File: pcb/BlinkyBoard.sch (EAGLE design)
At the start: 21 parts, among them Q1 16 MHz

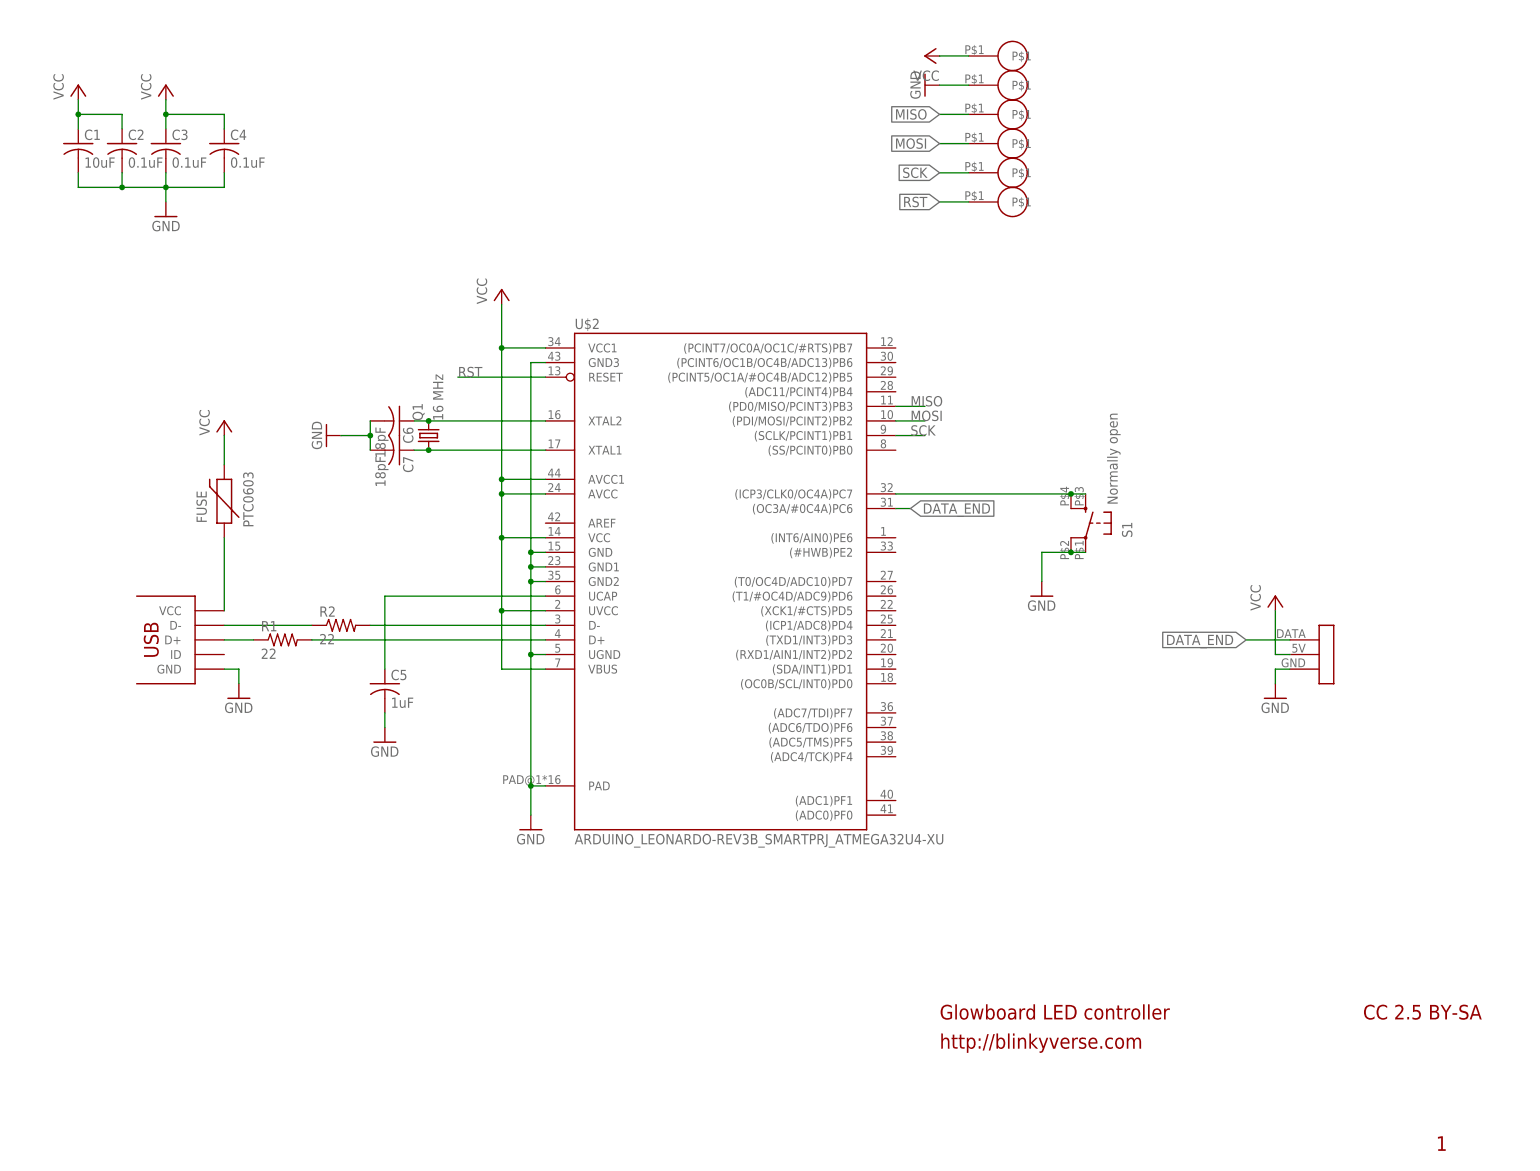
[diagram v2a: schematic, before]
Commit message: Add chopped version of 32u4 package, for BB RevB
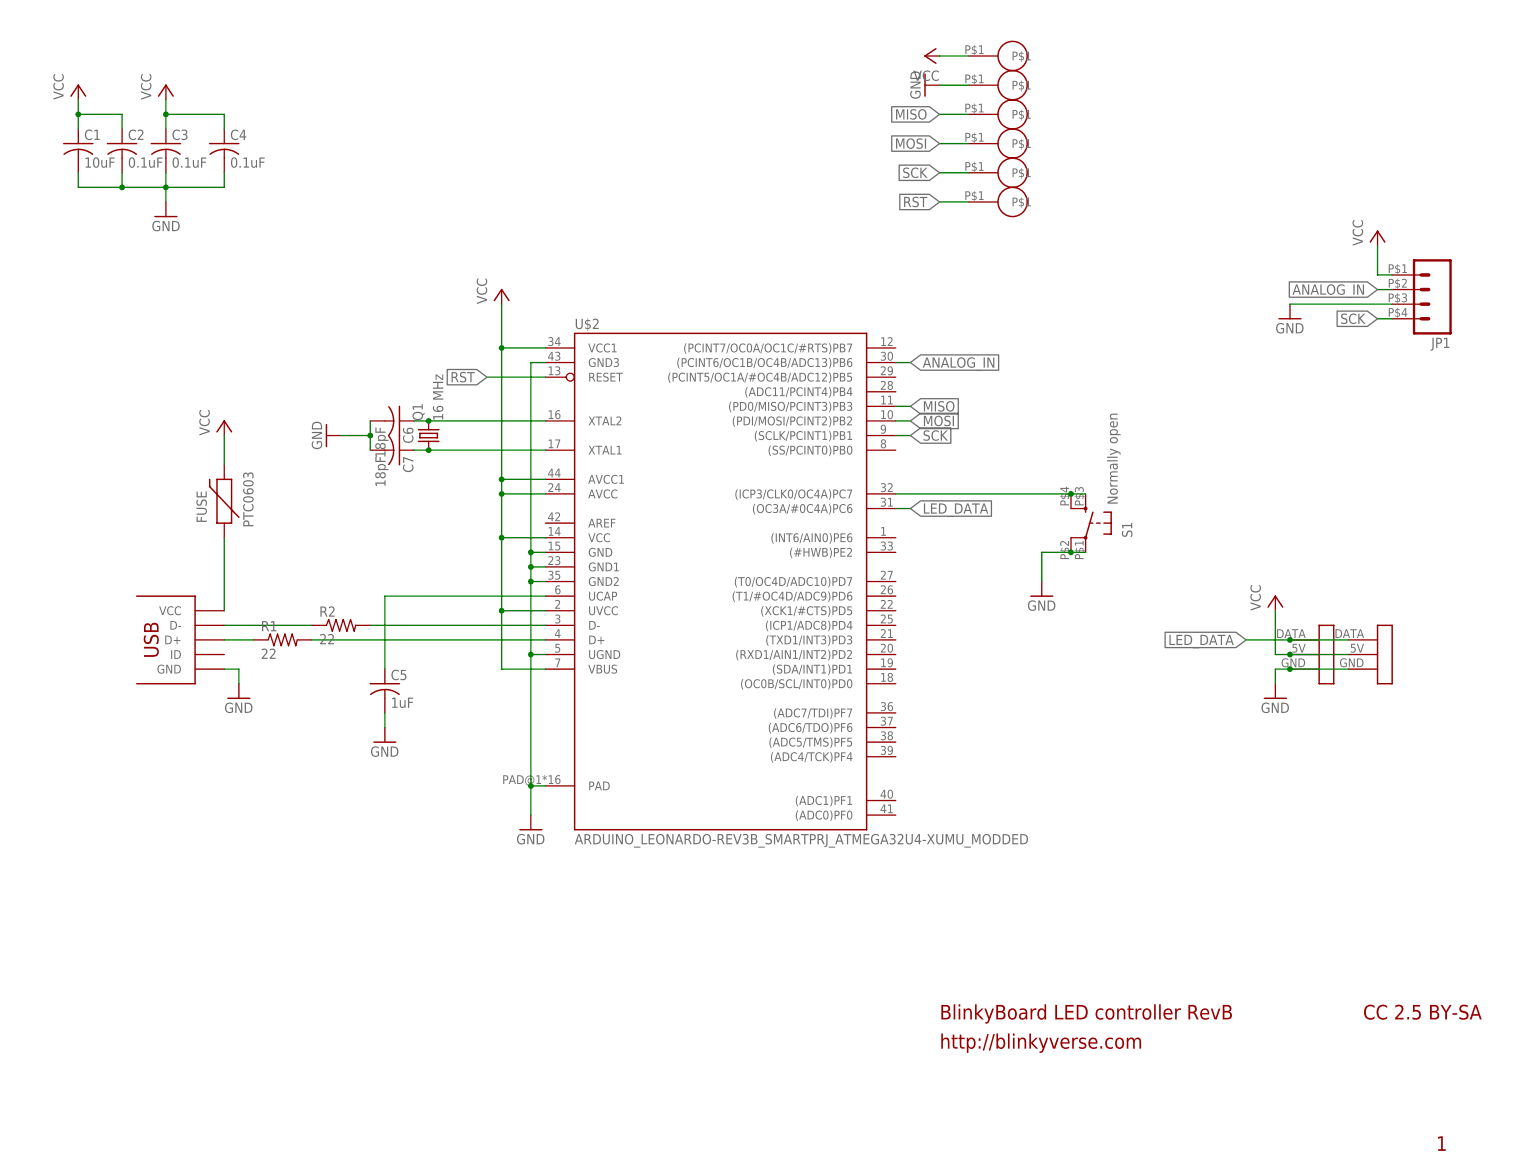
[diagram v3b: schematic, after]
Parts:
- added JP1: (no value), blinkiverse:M04
- added WS3: WS2811_CONNECTOR, blinkiverse:WS2811_CONNECTOR
- U$2: value ARDUINO_LEONARDO-REV3B_SMARTPRJ_ATMEGA32U4-XU -> ARDUINO_LEONARDO-REV3B_SMARTPRJ_ATMEGA32U4-XUMU_MODDED; device blinkiverse:ARDUINO_LEONARDO-REV3B_SMARTPRJ_ATMEGA32U4-XU -> blinkiverse:ARDUINO_LEONARDO-REV3B_SMARTPRJ_ATMEGA32U4-XUMU_MODDED
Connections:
- removed net DATA_END: U$2.(OC3A/#0C4A)PC6, WS1.DATA
- new net ANALOG_IN: JP1.2, U$2.(PCINT6/OC1B/OC4B/ADC13)PB6
- new net LED_DATA: U$2.(OC3A/#0C4A)PC6, WS1.DATA, WS3.DATA
- net GND: now also JP1.3, WS3.GND
- net SCK: now also JP1.4
- net VCC: now also JP1.1, WS3.5V
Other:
- note added: "BlinkyBoard LED controller RevB"
- note removed: "Glowboard LED controller"
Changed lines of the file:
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@@
 <setting verticaltext="up"/>
 </settings>
-<grid distance="0.1" unitdist="inch" unit="inch" style="lines" multiple="1" display="yes" altdistance="0.01" altunitdist="inch" altunit="inch"/>
+<grid distance="0.1" unitdist="inch" unit="inch" style="lines" multiple="1" display="no" altdistance="0.01" altunitdist="inch" altunit="inch"/>
 <layers>
 <layer number="1" name="Top" color="4" fill="1" visible="no" active="no"/>
@@
 <part name="P+1" library="supply1" deviceset="VCC" device=""/>
 <part name="FRAME1" library="frames" deviceset="FRAME_A_L" device=""/>
-<part name="U$2" library="blinkiverse" deviceset="ARDUINO_LEONARDO-REV3B_SMARTPRJ_ATMEGA32U4-XU" device="" value="ARDUINO_LEONARDO-REV3B_SMARTPRJ_ATMEGA32U4-XU"/>
+<part name="U$2" library="blinkiverse" deviceset="ARDUINO_LEONARDO-REV3B_SMARTPRJ_ATMEGA32U4-XU" device="MU_MODDED" value="ARDUINO_LEONARDO-REV3B_SMARTPRJ_ATMEGA32U4-XUMU_MODDED"/>
 <part name="GND8" library="supply1" deviceset="GND" device=""/>
 <part name="P+6" library="supply1" deviceset="VCC" device=""/>
@@
 <part name="P+2" library="supply1" deviceset="VCC" device=""/>
 <part name="GND1" library="supply1" deviceset="GND" device=""/>
+<part name="GND2" library="supply1" deviceset="GND" device=""/>
+<part name="WS3" library="blinkiverse" deviceset="WS2811_CONNECTOR" device=""/>
+<part name="JP1" library="blinkiverse" deviceset="M04" device=""/>
+<part name="P+5" library="supply1" deviceset="VCC" device=""/>
 </parts>
 <sheets>
 <sheet>
 <plain>
-<text x="104.14" y="-30.48" size="2.54" layer="94">Glowboard LED controller</text>
+<text x="104.14" y="-30.48" size="2.54" layer="94">BlinkyBoard LED controller RevB</text>
 <text x="104.14" y="-35.56" size="2.54" layer="94">http://blinkyverse.com</text>
 <text x="177.8" y="-30.48" size="2.54" layer="94">CC 2.5 BY-SA</text>
@@
 <instance part="P+2" gate="VCC" x="101.6" y="137.16" rot="R90"/>
 <instance part="GND1" gate="1" x="101.6" y="132.08" rot="R270"/>
+<instance part="GND2" gate="1" x="165.1" y="91.44"/>
+<instance part="WS3" gate="G$1" x="182.88" y="33.02"/>
+<instance part="JP1" gate="G$1" x="187.96" y="96.52" rot="R180"/>
+<instance part="P+5" gate="VCC" x="180.34" y="106.68"/>
 </instances>
 <busses>
@@
 <pinref part="GND4" gate="1" pin="GND"/>
 <wire x1="162.56" y1="30.48" x2="162.56" y2="27.94" width="0.1524" layer="91"/>
+<pinref part="WS3" gate="G$1" pin="GND"/>
+<wire x1="175.26" y1="30.48" x2="165.1" y2="30.48" width="0.1524" layer="91"/>
+<junction x="165.1" y="30.48"/>
 </segment>
 <segment>
@@
 <wire x1="104.14" y1="132.08" x2="109.22" y2="132.08" width="0.1524" layer="91"/>
 </segment>
+<segment>
+<pinref part="GND2" gate="1" pin="GND"/>
+<wire x1="165.1" y1="93.98" x2="182.88" y2="93.98" width="0.1524" layer="91"/>
+<pinref part="JP1" gate="G$1" pin="3"/>
+</segment>
 </net>
 <net name="MOSI" class="0">
 <segment>
 <pinref part="U$2" gate="G$1" pin="(PDI/MOSI/PCINT2)PB2"/>
-<wire x1="96.52" y1="73.66" x2="101.6" y2="73.66" width="0.1524" layer="91"/>
-<label x="99.06" y="73.66" size="1.778" layer="95"/>
+<wire x1="96.52" y1="73.66" x2="99.06" y2="73.66" width="0.1524" layer="91"/>
+<label x="99.06" y="73.66" size="1.778" layer="95" xref="yes"/>
 </segment>
 <segment>
@@
 <segment>
 <pinref part="U$2" gate="G$1" pin="(PD0/MISO/PCINT3)PB3"/>
-<wire x1="96.52" y1="76.2" x2="101.6" y2="76.2" width="0.1524" layer="91"/>
-<label x="99.06" y="76.2" size="1.778" layer="95"/>
+<wire x1="96.52" y1="76.2" x2="99.06" y2="76.2" width="0.1524" layer="91"/>
+<label x="99.06" y="76.2" size="1.778" layer="95" xref="yes"/>
 </segment>
 <segment>
@@
 <segment>
 <pinref part="U$2" gate="G$1" pin="(SCLK/PCINT1)PB1"/>
-<wire x1="96.52" y1="71.12" x2="101.6" y2="71.12" width="0.1524" layer="91"/>
-<label x="99.06" y="71.12" size="1.778" layer="95"/>
+<wire x1="96.52" y1="71.12" x2="99.06" y2="71.12" width="0.1524" layer="91"/>
+<label x="99.06" y="71.12" size="1.778" layer="95" xref="yes"/>
 </segment>
 <segment>
@@
 <pinref part="U$5" gate="G$1" pin="P$1"/>
 </segment>
+<segment>
+<pinref part="JP1" gate="G$1" pin="4"/>
+<wire x1="182.88" y1="91.44" x2="180.34" y2="91.44" width="0.1524" layer="91"/>
+<label x="180.34" y="91.44" size="1.778" layer="95" rot="R180" xref="yes"/>
+</segment>
 </net>
 <net name="RST" class="0">
 <segment>
 <pinref part="U$2" gate="G$1" pin="RESET"/>
-<wire x1="35.56" y1="81.28" x2="20.32" y2="81.28" width="0.1524" layer="91"/>
-<label x="20.32" y="81.28" size="1.778" layer="95"/>
+<wire x1="35.56" y1="81.28" x2="25.4" y2="81.28" width="0.1524" layer="91"/>
+<label x="25.4" y="81.28" size="1.778" layer="95" rot="R180" xref="yes"/>
 </segment>
 <segment>
@@
 </segment>
 </net>
+<net name="D-" class="0">
+<segment>
+<pinref part="R2" gate="G$1" pin="2"/>
+<pinref part="U$2" gate="G$1" pin="D-"/>
+<wire x1="5.08" y1="38.1" x2="35.56" y2="38.1" width="0.1524" layer="91"/>
+</segment>
+</net>
+<net name="D+" class="0">
+<segment>
+<pinref part="U$2" gate="G$1" pin="D+"/>
+<pinref part="R1" gate="G$1" pin="2"/>
+<wire x1="35.56" y1="35.56" x2="-5.08" y2="35.56" width="0.1524" layer="91"/>
+</segment>
+</net>
+<net name="N$10" class="0">
+<segment>
+<pinref part="U$2" gate="G$1" pin="(ICP3/CLK0/OC4A)PC7"/>
+<pinref part="S1" gate="1" pin="S1"/>
+<wire x1="96.52" y1="60.96" x2="127" y2="60.96" width="0.1524" layer="91"/>
+<pinref part="S1" gate="1" pin="S"/>
+<wire x1="129.54" y1="60.96" x2="127" y2="60.96" width="0.1524" layer="91"/>
+<junction x="127" y="60.96"/>
+</segment>
+</net>
+<net name="N$1" class="0">
+<segment>
+<pinref part="FUSE" gate="G$1" pin="1"/>
+<pinref part="U$4" gate="G$1" pin="VCC"/>
+<wire x1="-20.32" y1="40.64" x2="-20.32" y2="53.34" width="0.1524" layer="91"/>
+</segment>
+</net>
+<net name="N$2" class="0">
+<segment>
+<pinref part="U$2" gate="G$1" pin="UCAP"/>
+<wire x1="35.56" y1="43.18" x2="7.62" y2="43.18" width="0.1524" layer="91"/>
+<pinref part="C5" gate="G$1" pin="1"/>
+<wire x1="7.62" y1="30.48" x2="7.62" y2="43.18" width="0.1524" layer="91"/>
+</segment>
+</net>
+<net name="ANALOG_IN" class="0">
+<segment>
+<pinref part="U$2" gate="G$1" pin="(PCINT6/OC1B/OC4B/ADC13)PB6"/>
+<wire x1="96.52" y1="83.82" x2="99.06" y2="83.82" width="0.1524" layer="91"/>
+<label x="99.06" y="83.82" size="1.778" layer="95" xref="yes"/>
+</segment>
+<segment>
+<label x="180.34" y="96.52" size="1.778" layer="95" rot="R180" xref="yes"/>
+<pinref part="JP1" gate="G$1" pin="2"/>
+<wire x1="182.88" y1="96.52" x2="180.34" y2="96.52" width="0.1524" layer="91"/>
+</segment>
+</net>
+<net name="LED_DATA" class="0">
+<segment>
+<pinref part="U$2" gate="G$1" pin="(OC3A/#0C4A)PC6"/>
+<wire x1="96.52" y1="58.42" x2="99.06" y2="58.42" width="0.1524" layer="91"/>
+<label x="99.06" y="58.42" size="1.778" layer="95" xref="yes"/>
+</segment>
+<segment>
+<pinref part="WS1" gate="G$1" pin="DATA"/>
+<wire x1="165.1" y1="35.56" x2="157.48" y2="35.56" width="0.1524" layer="91"/>
+<label x="157.48" y="35.56" size="1.778" layer="95" rot="R180" xref="yes"/>
+<pinref part="WS3" gate="G$1" pin="DATA"/>
+<wire x1="175.26" y1="35.56" x2="165.1" y2="35.56" width="0.1524" layer="91"/>
+<junction x="165.1" y="35.56"/>
+</segment>
+</net>
 <net name="VCC" class="0">
+<segment>
+<pinref part="JP1" gate="G$1" pin="1"/>
+<wire x1="182.88" y1="99.06" x2="180.34" y2="99.06" width="0.1524" layer="91"/>
+<wire x1="180.34" y1="99.06" x2="180.34" y2="104.14" width="0.1524" layer="91"/>
+<pinref part="P+5" gate="VCC" pin="VCC"/>
+</segment>
 <segment>
 <pinref part="C1" gate="G$1" pin="1"/>
@@
 <pinref part="P+3" gate="VCC" pin="VCC"/>
 <wire x1="162.56" y1="33.02" x2="162.56" y2="40.64" width="0.1524" layer="91"/>
+<pinref part="WS3" gate="G$1" pin="5V"/>
+<wire x1="165.1" y1="33.02" x2="175.26" y2="33.02" width="0.1524" layer="91"/>
+<junction x="165.1" y="33.02"/>
 </segment>
 <segment>
@@
 </segment>
 </net>
-<net name="D-" class="0">
-<segment>
-<pinref part="R2" gate="G$1" pin="2"/>
-<pinref part="U$2" gate="G$1" pin="D-"/>
-<wire x1="5.08" y1="38.1" x2="35.56" y2="38.1" width="0.1524" layer="91"/>
-</segment>
-</net>
-<net name="D+" class="0">
-<segment>
-<pinref part="U$2" gate="G$1" pin="D+"/>
-<pinref part="R1" gate="G$1" pin="2"/>
-<wire x1="35.56" y1="35.56" x2="-5.08" y2="35.56" width="0.1524" layer="91"/>
-</segment>
-</net>
-<net name="N$10" class="0">
-<segment>
-<pinref part="U$2" gate="G$1" pin="(ICP3/CLK0/OC4A)PC7"/>
-<pinref part="S1" gate="1" pin="S1"/>
-<wire x1="96.52" y1="60.96" x2="127" y2="60.96" width="0.1524" layer="91"/>
-<pinref part="S1" gate="1" pin="S"/>
-<wire x1="129.54" y1="60.96" x2="127" y2="60.96" width="0.1524" layer="91"/>
-<junction x="127" y="60.96"/>
-</segment>
-</net>
-<net name="N$1" class="0">
-<segment>
-<pinref part="FUSE" gate="G$1" pin="1"/>
-<pinref part="U$4" gate="G$1" pin="VCC"/>
-<wire x1="-20.32" y1="40.64" x2="-20.32" y2="53.34" width="0.1524" layer="91"/>
-</segment>
-</net>
-<net name="N$2" class="0">
-<segment>
-<pinref part="U$2" gate="G$1" pin="UCAP"/>
-<wire x1="35.56" y1="43.18" x2="7.62" y2="43.18" width="0.1524" layer="91"/>
-<pinref part="C5" gate="G$1" pin="1"/>
-<wire x1="7.62" y1="30.48" x2="7.62" y2="43.18" width="0.1524" layer="91"/>
-</segment>
-</net>
-<net name="DATA_END" class="0">
-<segment>
-<pinref part="WS1" gate="G$1" pin="DATA"/>
-<wire x1="165.1" y1="35.56" x2="157.48" y2="35.56" width="0.1524" layer="91"/>
-<label x="157.48" y="35.56" size="1.778" layer="95" rot="R180" xref="yes"/>
-</segment>
-<segment>
-<pinref part="U$2" gate="G$1" pin="(OC3A/#0C4A)PC6"/>
-<wire x1="96.52" y1="58.42" x2="99.06" y2="58.42" width="0.1524" layer="91"/>
-<label x="99.06" y="58.42" size="1.778" layer="95" xref="yes"/>
-</segment>
-</net>

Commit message: Fuses are for suckers.
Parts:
- removed FUSE: PTC0603, SparkFun-PowerIC:PTC0603
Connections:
- removed net N$1: FUSE.1, U$4.VCC
- net VCC: now also U$4.VCC; no longer FUSE.2
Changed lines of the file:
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@@
 <part name="P+3" library="supply1" deviceset="VCC" device=""/>
 <part name="GND4" library="supply1" deviceset="GND" device=""/>
-<part name="FUSE" library="SparkFun-PowerIC" deviceset="PTC" device="0603"/>
 <part name="P+4" library="supply1" deviceset="VCC" device=""/>
 <part name="U$4" library="blinkiverse" deviceset="MICRO_USB" device=""/>
@@
 <instance part="P+3" gate="VCC" x="162.56" y="43.18"/>
 <instance part="GND4" gate="1" x="162.56" y="25.4"/>
-<instance part="FUSE" gate="G$1" x="-20.32" y="58.42" rot="R90"/>
 <instance part="P+4" gate="VCC" x="-20.32" y="73.66"/>
 <instance part="U$4" gate="G$1" x="-27.94" y="35.56"/>
@@
 <instance part="P+2" gate="VCC" x="101.6" y="137.16" rot="R90"/>
 <instance part="GND1" gate="1" x="101.6" y="132.08" rot="R270"/>
-<instance part="GND2" gate="1" x="165.1" y="91.44"/>
+<instance part="GND2" gate="1" x="170.18" y="86.36"/>
 <instance part="WS3" gate="G$1" x="182.88" y="33.02"/>
 <instance part="JP1" gate="G$1" x="187.96" y="96.52" rot="R180"/>
@@
 </segment>
 <segment>
+<pinref part="JP1" gate="G$1" pin="3"/>
 <pinref part="GND2" gate="1" pin="GND"/>
-<wire x1="165.1" y1="93.98" x2="182.88" y2="93.98" width="0.1524" layer="91"/>
-<pinref part="JP1" gate="G$1" pin="3"/>
+<wire x1="182.88" y1="93.98" x2="170.18" y2="93.98" width="0.1524" layer="91"/>
+<wire x1="170.18" y1="93.98" x2="170.18" y2="88.9" width="0.1524" layer="91"/>
 </segment>
 </net>
@@
 </segment>
 <segment>
+<label x="180.34" y="91.44" size="1.778" layer="95" rot="R180" xref="yes"/>
 <pinref part="JP1" gate="G$1" pin="4"/>
-<wire x1="182.88" y1="91.44" x2="180.34" y2="91.44" width="0.1524" layer="91"/>
-<label x="180.34" y="91.44" size="1.778" layer="95" rot="R180" xref="yes"/>
+<wire x1="180.34" y1="91.44" x2="182.88" y2="91.44" width="0.1524" layer="91"/>
 </segment>
 </net>
@@
 <wire x1="129.54" y1="60.96" x2="127" y2="60.96" width="0.1524" layer="91"/>
 <junction x="127" y="60.96"/>
-</segment>
-</net>
-<net name="N$1" class="0">
-<segment>
-<pinref part="FUSE" gate="G$1" pin="1"/>
-<pinref part="U$4" gate="G$1" pin="VCC"/>
-<wire x1="-20.32" y1="40.64" x2="-20.32" y2="53.34" width="0.1524" layer="91"/>
 </segment>
 </net>
@@
 </segment>
 <segment>
-<pinref part="FUSE" gate="G$1" pin="2"/>
-<wire x1="-20.32" y1="66.04" x2="-20.32" y2="71.12" width="0.1524" layer="91"/>
 <pinref part="P+4" gate="VCC" pin="VCC"/>
-</segment>
-<segment>
+<pinref part="U$4" gate="G$1" pin="VCC"/>
+<wire x1="-20.32" y1="71.12" x2="-20.32" y2="40.64" width="0.1524" layer="91"/>
+</segment>
+<segment>

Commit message: PCB: replace smt USB connector with thru-hole version
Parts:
- removed JP1: (no value), blinkiverse:M04
- U$4: value MICRO_USB -> MICRO_USBSMT+DIP; device blinkiverse:MICRO_USB -> blinkiverse:MICRO_USBSMT+DIP
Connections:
- net ANALOG_IN: no longer JP1.2
- net GND: no longer JP1.3
- net SCK: no longer JP1.4
- net VCC: no longer JP1.1
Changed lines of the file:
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@@
 <part name="GND4" library="supply1" deviceset="GND" device=""/>
 <part name="P+4" library="supply1" deviceset="VCC" device=""/>
-<part name="U$4" library="blinkiverse" deviceset="MICRO_USB" device=""/>
+<part name="U$4" library="blinkiverse" deviceset="MICRO_USB" device="SMT+DIP"/>
 <part name="GND5" library="supply1" deviceset="GND" device=""/>
 <part name="U$1" library="blinkiverse" deviceset="TEST_VIA" device=""/>
@@
 <part name="GND2" library="supply1" deviceset="GND" device=""/>
 <part name="WS3" library="blinkiverse" deviceset="WS2811_CONNECTOR" device=""/>
-<part name="JP1" library="blinkiverse" deviceset="M04" device=""/>
 <part name="P+5" library="supply1" deviceset="VCC" device=""/>
 </parts>
@@
 <instance part="GND2" gate="1" x="170.18" y="86.36"/>
 <instance part="WS3" gate="G$1" x="182.88" y="33.02"/>
-<instance part="JP1" gate="G$1" x="187.96" y="96.52" rot="R180"/>
 <instance part="P+5" gate="VCC" x="180.34" y="106.68"/>
 </instances>
@@
 </segment>
 <segment>
-<pinref part="JP1" gate="G$1" pin="3"/>
 <pinref part="GND2" gate="1" pin="GND"/>
 <wire x1="182.88" y1="93.98" x2="170.18" y2="93.98" width="0.1524" layer="91"/>
@@
 <segment>
 <label x="180.34" y="91.44" size="1.778" layer="95" rot="R180" xref="yes"/>
-<pinref part="JP1" gate="G$1" pin="4"/>
 <wire x1="180.34" y1="91.44" x2="182.88" y2="91.44" width="0.1524" layer="91"/>
 </segment>
@@
 <segment>
 <label x="180.34" y="96.52" size="1.778" layer="95" rot="R180" xref="yes"/>
-<pinref part="JP1" gate="G$1" pin="2"/>
 <wire x1="182.88" y1="96.52" x2="180.34" y2="96.52" width="0.1524" layer="91"/>
 </segment>
@@
 <net name="VCC" class="0">
 <segment>
-<pinref part="JP1" gate="G$1" pin="1"/>
 <wire x1="182.88" y1="99.06" x2="180.34" y2="99.06" width="0.1524" layer="91"/>
 <wire x1="180.34" y1="99.06" x2="180.34" y2="104.14" width="0.1524" layer="91"/>
